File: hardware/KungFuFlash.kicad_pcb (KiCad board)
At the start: 2 copper layers, 60.6 x 62 mm, 40 parts, among them J1 USB Power, J2 USB_B_Micro, J4 SWD, Q1 BC817, SW1 Reset, SW2 Menu, SW3 Special, U1 C64-Exp-Port, U2 AMS1117-3.3, U3 STM32F405RGTx, Y1 8MHz

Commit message: Long board cart PCB layout.
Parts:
- removed RN1, RN2: 100R, Resistor_SMD:R_Array_Convex_4x0603
- added R10: 100R, Resistor_SMD:R_0805_2012Metric_Pad1.15x1.40mm_HandSolder, F.Cu at (116.1, 130.4)
- added R11: 100R, Resistor_SMD:R_0805_2012Metric_Pad1.15x1.40mm_HandSolder, F.Cu at (118.7, 130.4)
- added R12: 100R, Resistor_SMD:R_0805_2012Metric_Pad1.15x1.40mm_HandSolder, F.Cu at (121.2, 130.4)
- added R13: 100R, Resistor_SMD:R_0805_2012Metric_Pad1.15x1.40mm_HandSolder, F.Cu at (123.8, 130.4)
- added R14: 100R, Resistor_SMD:R_0805_2012Metric_Pad1.15x1.40mm_HandSolder, F.Cu at (126.3, 130.4)
- added R7: 100R, Resistor_SMD:R_0805_2012Metric_Pad1.15x1.40mm_HandSolder, F.Cu at (108.5, 130.4)
- added R8: 100R, Resistor_SMD:R_0805_2012Metric_Pad1.15x1.40mm_HandSolder, F.Cu at (111.1, 130.4)
- added R9: 100R, Resistor_SMD:R_0805_2012Metric_Pad1.15x1.40mm_HandSolder, F.Cu at (113.6, 130.4)
- J2: value USB_B_Micro -> USB_B_Mini; footprint mod:Conn_USBmicro-B_ebay-side_TH -> Connector_USB:USB_Mini-B_Wuerth_65100516121_Horizontal
- SW1, SW2, SW3: footprint Button_Switch_THT:SW_PUSH_6mm_H8mm -> Button_Switch_THT:SW_Tactile_SPST_Angled_PTS645Vx83-2LFS
- moved C11 19.3 mm to (92.3, 124.3)
- moved R4 16.8 mm to (85.7, 128.4)
- moved U1 14.3 mm to (73.0, 144.1)
- moved C4 14.3 mm to (92.2, 113.2)
- moved R3 14.1 mm to (85.7, 125.1), turned to 0 degrees
- moved U3 13.9 mm to (103.2, 115.7)
- moved J1 13.0 mm to (122.7, 99.4), turned to 180 degrees
- moved REF** 12.9 mm to (122.7, 122.8)
- moved C3 12.3 mm to (88.2, 117.5)
- moved Q1 12.2 mm to (80.6, 127.6)
- moved C1 12.1 mm to (76.8, 117.2)
- moved U2 11.9 mm to (82.4, 115.5), turned to 90 degrees
- moved C14 11.8 mm to (101.5, 104.8)
- moved C2 11.7 mm to (82.4, 108.3), turned to 0 degrees
- moved C5 11.4 mm to (92.1, 119.0), turned to 0 degrees
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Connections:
- J2 pad 4: Net-(J2-Pad4) -> (no net)
- U1 pad 13: Net-(U1-Pad13) -> (no net)
- U1 pad 6: Net-(U1-Pad6) -> (no net)
- XS1 pad 9: Net-(XS1-Pad9) -> (no net)
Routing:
- net GND: track 751.1 -> 0.00 mm, vias 66 -> 0
- net +3V3: track 232.6 -> 0.00 mm, vias 8 -> 0
- net +5V: track 99.0 -> 0.00 mm, vias 2 -> 0
- net /A0: track 50.3 -> 0.00 mm, vias 1 -> 0
- net /A1: track 46.8 -> 0.00 mm, vias 1 -> 0
- net /USB_DP: track 45.1 -> 0.00 mm
- net /USB_DM: track 44.6 -> 0.00 mm
- net /R~W: track 44.5 -> 0.00 mm, vias 2 -> 0
- net /A2: track 43.6 -> 0.00 mm, vias 1 -> 0
- net /~RST_O: track 43.0 -> 0.00 mm, vias 2 -> 0
- net /D0: track 41.1 -> 0.00 mm, vias 2 -> 0
- net /D1: track 40.1 -> 0.00 mm, vias 2 -> 0
- net /D2: track 39.3 -> 0.00 mm, vias 2 -> 0
- net /D3: track 38.9 -> 0.00 mm, vias 2 -> 0
- net /~IO1: track 38.5 -> 0.00 mm, vias 2 -> 0
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- removed copper zone on B.Cu, net GND
- removed copper zone on F.Cu, net GND
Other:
- board size 60.6 x 62 mm -> 62 x 83.6 mm
- board text added: "Rev. 2 LONG"
- board text removed: "+"
- board text removed: "Rev. 2"

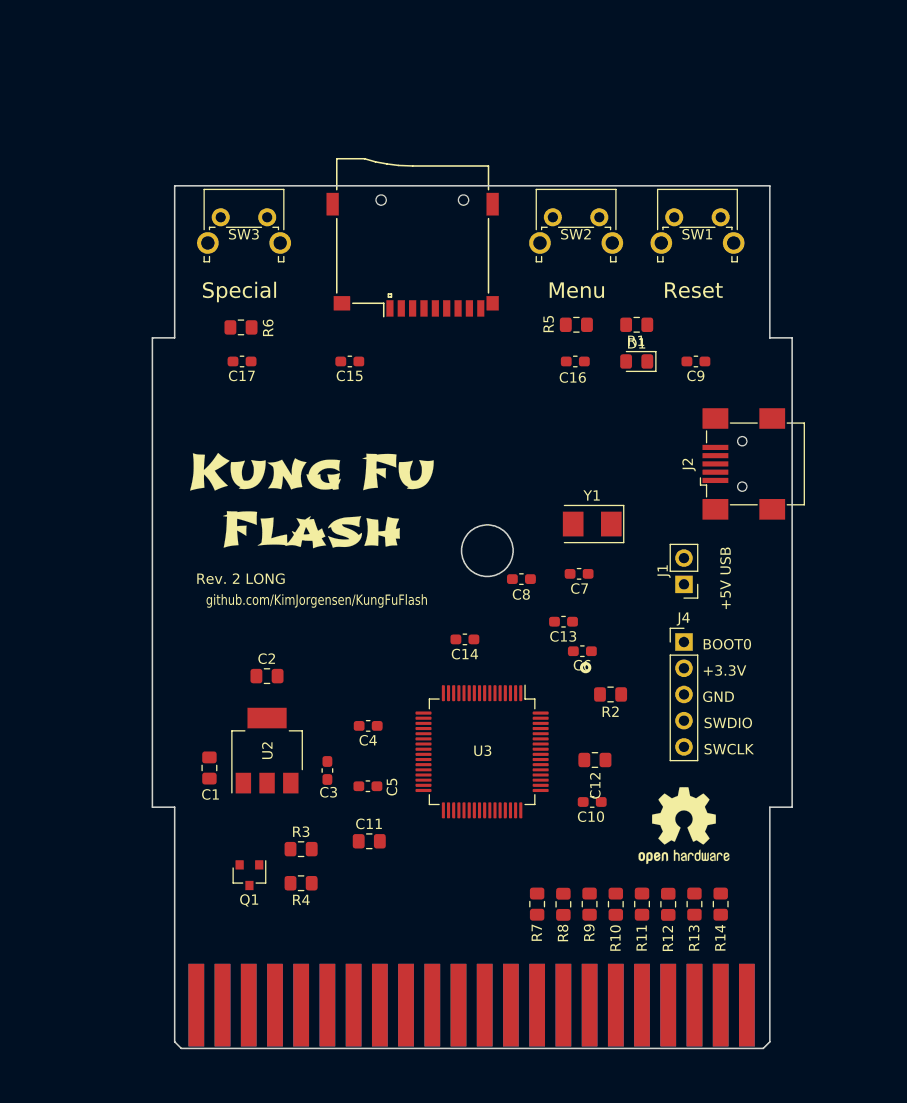
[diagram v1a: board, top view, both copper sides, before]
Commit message: Trace routing and layout cleanup.
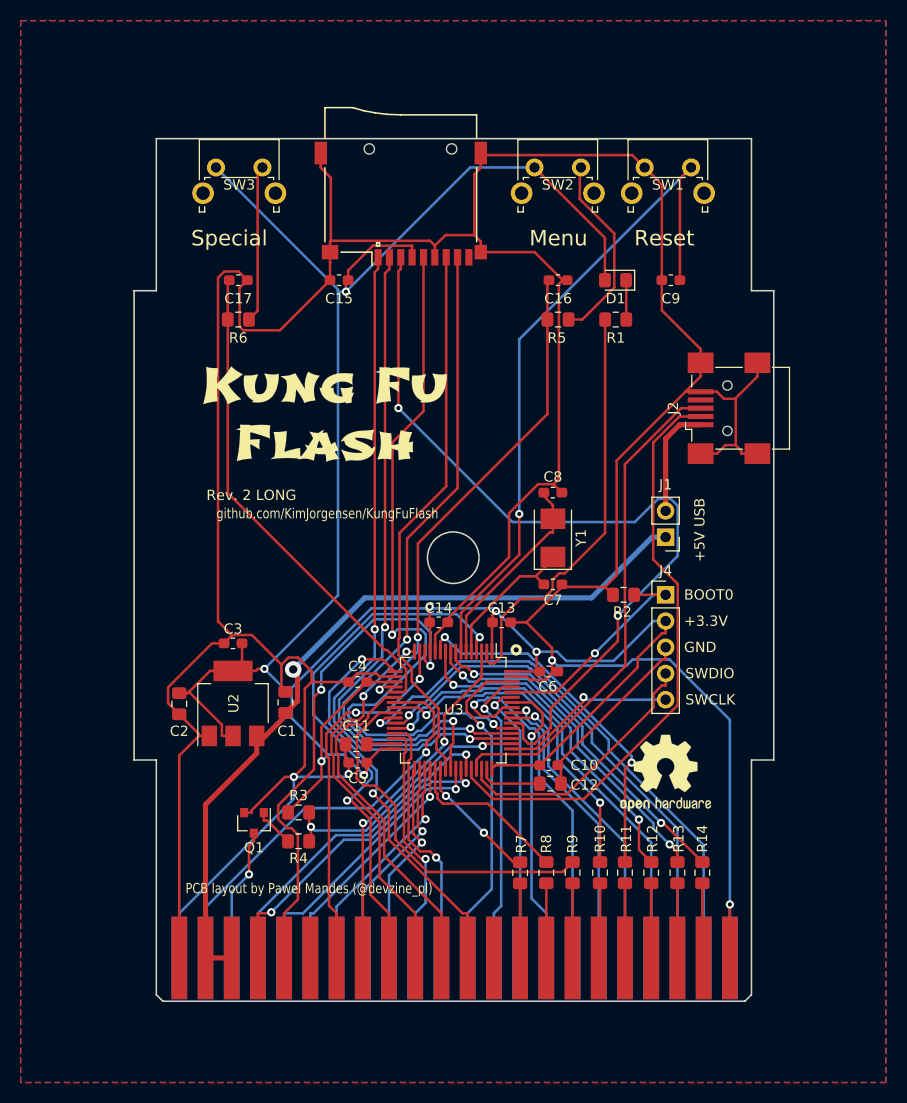
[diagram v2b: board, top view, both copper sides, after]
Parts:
- moved C3 15.3 mm to (79.1, 105.2), turned to 180 degrees
- moved R2 9.73 mm to (116.9, 100.5), turned to 180 degrees
- moved C1 9.73 mm to (84.1, 110.9)
- moved C11 9.48 mm to (91.0, 114.9)
- moved C8 8.92 mm to (110.0, 90.6)
- moved C2 8.91 mm to (73.9, 111.0), turned to 270 degrees
- moved G*** 8.48 mm to (87.9, 82.9)
- moved C9 8.24 mm to (121.5, 70.0)
- moved D1 8.14 mm to (116.1, 70.0)
- moved C16 8.05 mm to (110.5, 70.0)
- moved C15 7.94 mm to (89.3, 70.0)
- moved C17 7.88 mm to (79.6, 70.0), turned to 0 degrees
- moved C13 6.00 mm to (105.1, 103.1)
- moved U2 5.64 mm to (79.1, 111.0)
- moved SW1 5.61 mm to (118.9, 59.1)
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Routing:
- net GND: track 0.00 -> 425.5 mm, vias 0 -> 4
- net +3V3: track 0.00 -> 243.5 mm, vias 0 -> 7
- net /SD_CMD: track 0.00 -> 80.1 mm, vias 0 -> 2
- net +5V: track 0.00 -> 76.6 mm, vias 0 -> 1
- net /SD_CK: track 0.00 -> 71.9 mm, vias 0 -> 2
- net /~RST: track 0.00 -> 67.5 mm, vias 0 -> 1
- net /SD_D1: track 0.00 -> 66.2 mm, vias 0 -> 2
- net /SD_D2: track 0.00 -> 65.9 mm, vias 0 -> 2
- net /SD_D3: track 0.00 -> 65.4 mm, vias 0 -> 2
- net /USB_DM: track 0.00 -> 57.5 mm
- net /A0: track 0.00 -> 54.3 mm, vias 0 -> 1
- net /~EXROM: track 0.00 -> 54.0 mm, vias 0 -> 2
- net /SD_D0: track 0.00 -> 53.5 mm
- net /A1: track 0.00 -> 49.6 mm, vias 0 -> 1
- net /R~W: track 0.00 -> 49.1 mm, vias 0 -> 2
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- added copper zone on B.Cu, net GND
- added copper zone on F.Cu, net GND
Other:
- outline, holes or cut-outs redrawn
- board text added: "PCB layout by Pawel Mandes (@devzine_pl)"
